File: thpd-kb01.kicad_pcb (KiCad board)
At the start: 4 copper layers, 388 x 116 mm, 344 parts, among them J1 USB_C_Receptacle_USB2.0, SW1 SW_Push, SW2 SW_SPDT, SW3 Rotary_Encoder_Switch, U1 XC6206PxxxMR, U2 USBLC6-2SC6, U3 NHD-C12832A1Z, U4 STM32F072C8Tx

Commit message: Add art.
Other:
- board text added: "Rev. 1.0"
- board text added: "thpd-kb01"
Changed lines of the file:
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@@
   (general
     (thickness 1.6)
-    (drawings 6)
+    (drawings 21)
     (tracks 2110)
     (zones 0)
@@
     )
   )
+  (gr_line (start 104.5 183.5) (end 103.5 183.5) (layer F.SilkS) (width 0.2))
+  (gr_line (start 108.5 187.5) (end 108.5 188.5) (layer F.SilkS) (width 0.2))
+  (gr_line (start 105 187) (end 101 191) (layer F.SilkS) (width 0.2))
+  (gr_line (start 109.5 182.5) (end 108.5 183.5) (layer F.SilkS) (width 0.2))
+  (gr_line (start 109.5 184.5) (end 109.5 182.5) (layer F.SilkS) (width 0.2))
+  (gr_line (start 109.5 182.5) (end 109.5 184.5) (layer F.SilkS) (width 0.12))
+  (gr_line (start 107.5 182.5) (end 109.5 182.5) (layer F.SilkS) (width 0.2))
+  (gr_line (start 108.5 183.5) (end 108.5 187.5) (layer F.SilkS) (width 0.2))
+  (gr_line (start 104.5 183.5) (end 108.5 183.5) (layer F.SilkS) (width 0.2))
+  (gr_line (start 102.5 189.5) (end 102.5 184.5) (layer F.SilkS) (width 0.2))
+  (gr_line (start 107.5 189.5) (end 102.5 189.5) (layer F.SilkS) (width 0.2))
+  (gr_line (start 107.5 184.5) (end 107.5 189.5) (layer F.SilkS) (width 0.2))
+  (gr_line (start 102.5 184.5) (end 107.5 184.5) (layer F.SilkS) (width 0.2))
+  (gr_text "Rev. 1.0" (at 171 186.2) (layer F.SilkS)
+    (effects (font (size 2 2) (thickness 0.3)))
+  )
+  (gr_text thpd-kb01 (at 119.5 186.2) (layer F.SilkS)
+    (effects (font (size 2 2) (thickness 0.3)))
+  )
   (gr_line (start 404 81) (end 404 84) (layer Edge.Cuts) (width 0.05))

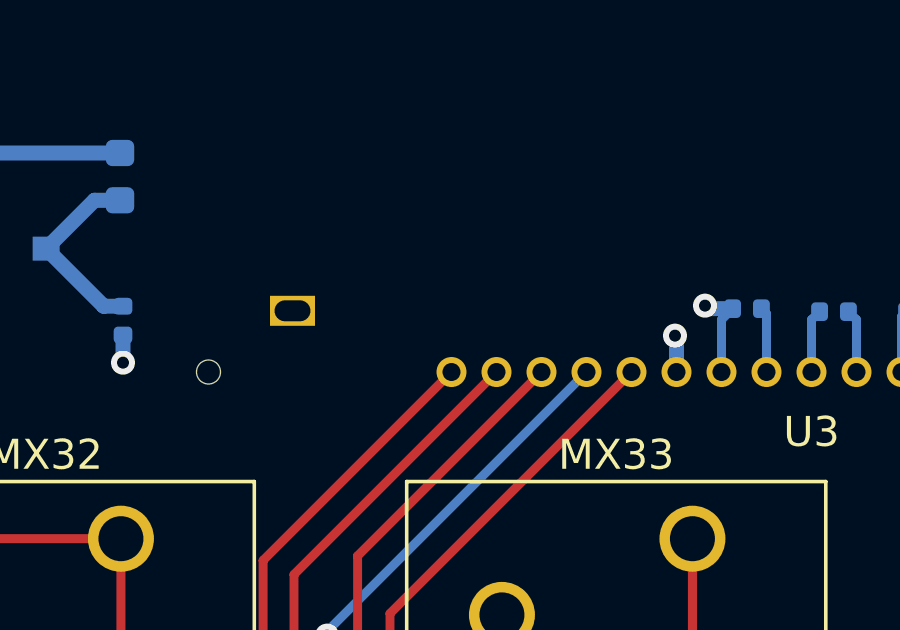
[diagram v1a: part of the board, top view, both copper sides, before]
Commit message: Add LCSC part numbers and prepared for output.
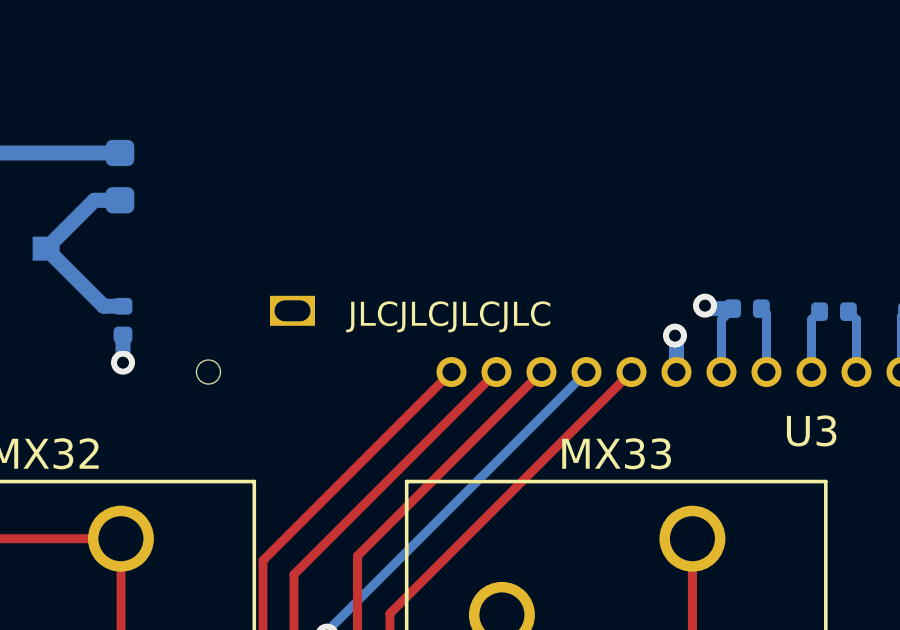
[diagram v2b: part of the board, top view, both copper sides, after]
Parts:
- R10: value 500 -> 510
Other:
- board text added: "JLCJLCJLCJLC"

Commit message: Remove LEDs and redo routing from scratch.
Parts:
- removed LED1, LED10, LED100, LED101, LED11, LED12, LED13, LED14, LED15, LED16, LED17, LED18, LED19, LED2, LED20, LED21, LED22, LED23, LED24, LED25, LED26, LED27, LED28, LED29, LED3, LED30, LED31, LED32, LED33, LED34, LED35, LED36, LED37, LED38, LED39, LED4, LED40, LED41, LED42, LED43, LED44, LED45, LED46, LED47, LED48, LED49, LED5, LED50, LED51, LED52, LED53, LED54, LED55, LED56, LED57, LED58, LED59, LED6, LED60, LED61, LED62, LED63, LED64, LED65, LED66, LED67, LED68, LED69, LED7, LED70, LED71, LED72, LED73, LED74, LED75, LED76, LED77, LED78, LED79, LED8, LED80, LED81, LED82, LED83, LED84, LED85, LED86, LED87, LED88, LED89, LED9, LED90, LED91, LED92, LED93, LED94, LED95, LED96, LED97, LED98, LED99: SK6812, thpd-kb01-custom:LED_SK6812MINI-ER_PLCC4_3.5x2.8mm_P1.8mm
- removed R10: 510, Resistor_SMD:R_0402_1005Metric
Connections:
- U4 pad 11: (no net) -> ROW3
- U4 pad 12: /led_matrix/DIN -> ROW4
- U4 pad 5: ROW3 -> (no net)
- U4 pad 6: ROW4 -> (no net)
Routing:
- net Net-(LED1-Pad2): track 401.5 -> 0.00 mm, vias 3 -> 0
- net Net-(LED35-Pad4): track 398.5 -> 0.00 mm, vias 2 -> 0
- net Net-(LED54-Pad4): track 397.3 -> 0.00 mm, vias 2 -> 0
- net Net-(LED89-Pad4): track 377.0 -> 0.00 mm, vias 2 -> 0
- net Net-(LED71-Pad4): track 374.8 -> 0.00 mm, vias 2 -> 0
- net Net-(LED16-Pad4): track 322.7 -> 0.00 mm, vias 2 -> 0
- net +3V3: track 135.4 -> 247.7 mm, vias 109 -> 8
- net Net-(LED92-Pad4): track 69.0 -> 0.00 mm, vias 2 -> 0
- net Net-(LED93-Pad4): track 66.6 -> 0.00 mm
- net Net-(LED67-Pad4): track 40.7 -> 0.00 mm
- net Net-(LED100-Pad2): track 31.7 -> 0.00 mm, vias 2 -> 0
- net Net-(LED72-Pad4): track 28.5 -> 0.00 mm
- net Net-(LED48-Pad4): track 27.7 -> 0.00 mm
- net Net-(LED30-Pad4): track 26.1 -> 0.00 mm
- net Net-(LED29-Pad4): track 26.1 -> 0.00 mm
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- removed copper zone on In2.Cu, net +3V3
- removed copper zone on In1.Cu, net GND
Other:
- copper layers 4 -> 2
- rule trace_min: 0.09 -> 0.127
- rule via_min_drill: 0.2 -> 0.3
- rule via_min_size: 0.4 -> 0.6

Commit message: All DRC errors corrected.
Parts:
- moved R1 2.65 mm to (323.5, 91.0), turned to 180 degrees
- moved R2 2.63 mm to (331.7, 91.1), turned to 180 degrees
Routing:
- net GND: track 266.3 -> 160.3 mm, vias 9 -> 4
- net Net-(J1-PadA5): track 1.85 -> 4.53 mm
- net Net-(J1-PadB5): track 1.85 -> 4.24 mm
- net D_USB_CONN+: track 8.16 -> 10.1 mm
- net COL10: track 200.3 -> 202.2 mm
- net D_USB_CONN-: track 8.49 -> 10.1 mm
- net COL9: track 219.5 -> 220.7 mm
- net +5V: track 25.8 -> 24.7 mm, vias 4 -> 3
- net COL15: track 128.8 -> 129.0 mm, vias 1 -> 2
- added copper zone on B.Cu, net GND
